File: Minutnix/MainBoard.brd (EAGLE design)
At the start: 222.3 x 73.3 mm, 121 parts, among them IC3 TP4056, IC7 FT232RL, Q4 32.768kHz, X1 FH12-12S-0.5S_THINNER, X2 JST-XH-03-PIN-LONG-PAD, X4 JST-XH-03-PIN-LONG-PAD

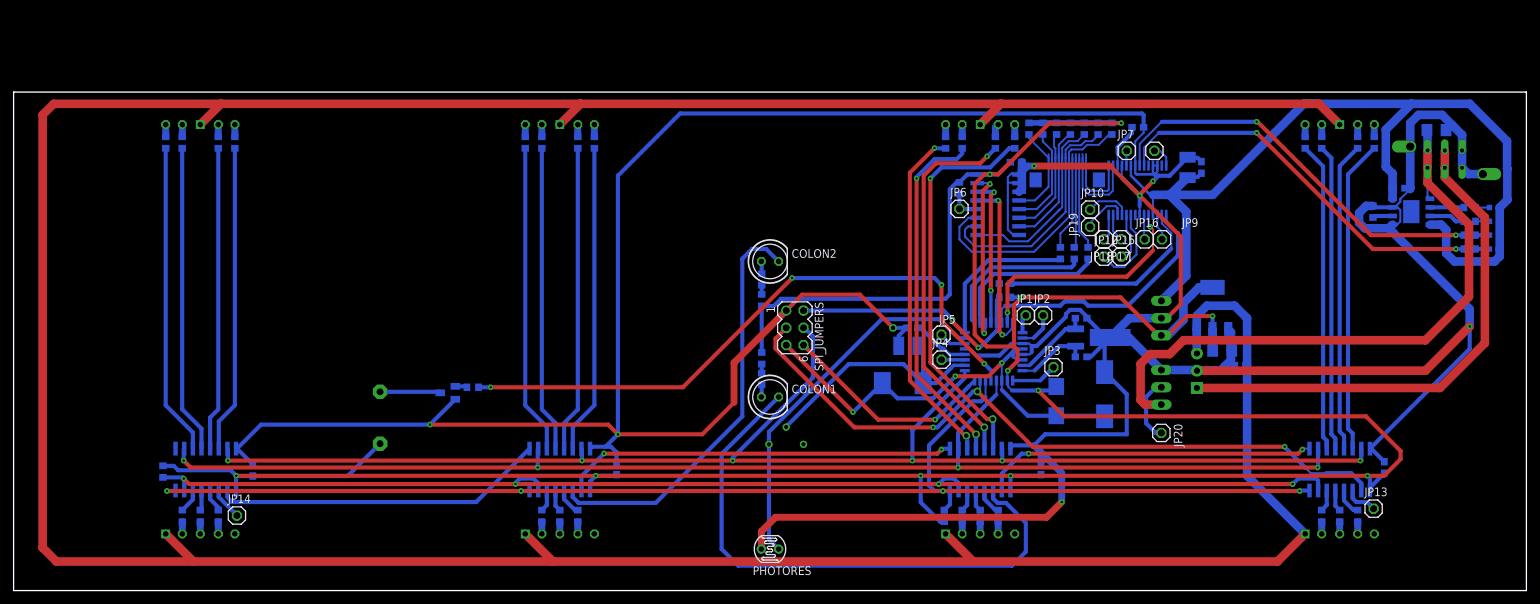
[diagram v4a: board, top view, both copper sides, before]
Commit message: Almost complete
Added 3d extraction
wider better paths
corrected Temperature field of TP to be GND
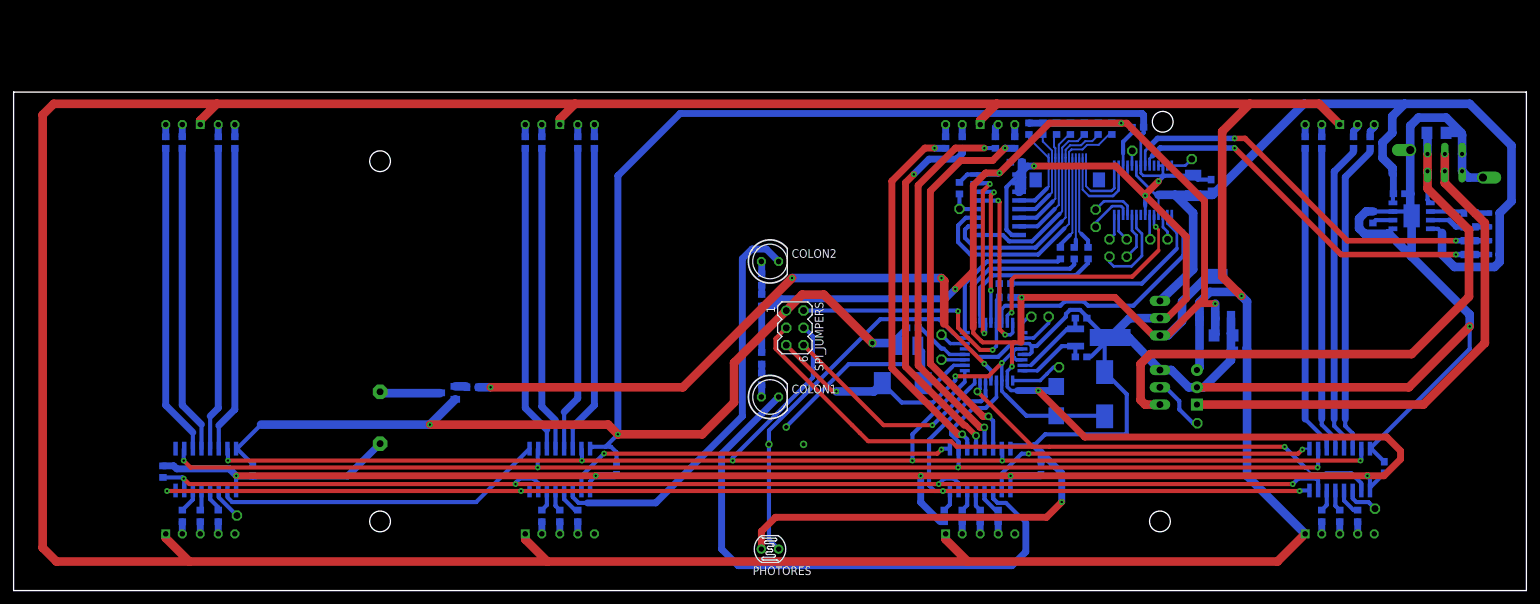
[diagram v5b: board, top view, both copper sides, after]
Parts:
- moved JP8 5.62 mm to (173.1, 63.4), flipped to the bottom
- moved JP20 5.47 mm to (173.9, 24.6), flipped to the bottom
- moved C5 3.00 mm to (176.0, 59.5)
- moved C3 2.76 mm to (173.3, 59.5)
- moved J_REG_9V_1 2.44 mm to (175.2, 29.9)
- moved C7 2.24 mm to (177.8, 37.5)
- moved C6 2.24 mm to (180.2, 35.4)
- moved IC2 1.68 mm to (176.6, 43.1)
- moved JP1 0.84 mm to (149.6, 40.2), flipped to the bottom
- moved JP2 0.84 mm to (152.1, 40.2), flipped to the bottom
- moved IC7 0.81 mm to (166.0, 58.8)
- moved JP12 0.81 mm to (161.0, 49.1), flipped to the bottom
- moved JP18 0.81 mm to (161.0, 51.6), flipped to the bottom
- moved JP3 0.81 mm to (153.6, 32.8), flipped to the bottom
- moved JP7 0.81 mm to (164.4, 64.6), flipped to the bottom
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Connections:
- net GND: now also IC3.ETP
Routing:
- net VDD: track 524.1 -> 559.9 mm, vias 0 -> 1
- net VCC: track 507.3 -> 528.5 mm, vias 11 -> 12
- net D_SI: track 105.2 -> 112.3 mm, vias 3 -> 2
- net GND: track 654.3 -> 661.2 mm
- net +5V: track 147.2 -> 143.6 mm
- net N$36: track 57.6 -> 54.3 mm
- net MS_G: track 51.0 -> 54.2 mm
- net N$43: track 59.1 -> 56.0 mm
- net RESET: track 38.9 -> 41.8 mm
- net MS_F: track 52.4 -> 54.4 mm
- net D_RCK: track 189.6 -> 191.5 mm
- net N$27: track 6.50 -> 8.33 mm
- net ENC_B: track 40.9 -> 42.6 mm
- net S_VCC: track 67.6 -> 66.0 mm
- net BATTERY_S: track 9.51 -> 8.39 mm
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
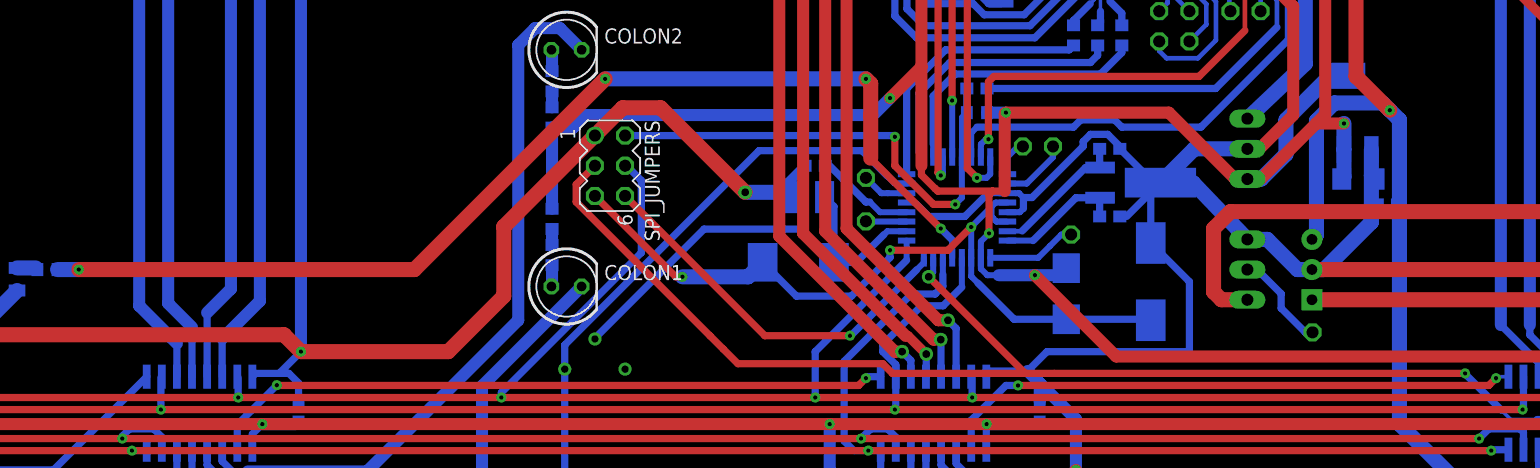
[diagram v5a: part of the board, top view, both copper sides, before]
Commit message: Corrected programmer pins
+ added full inventor 3d model with most important dimensions
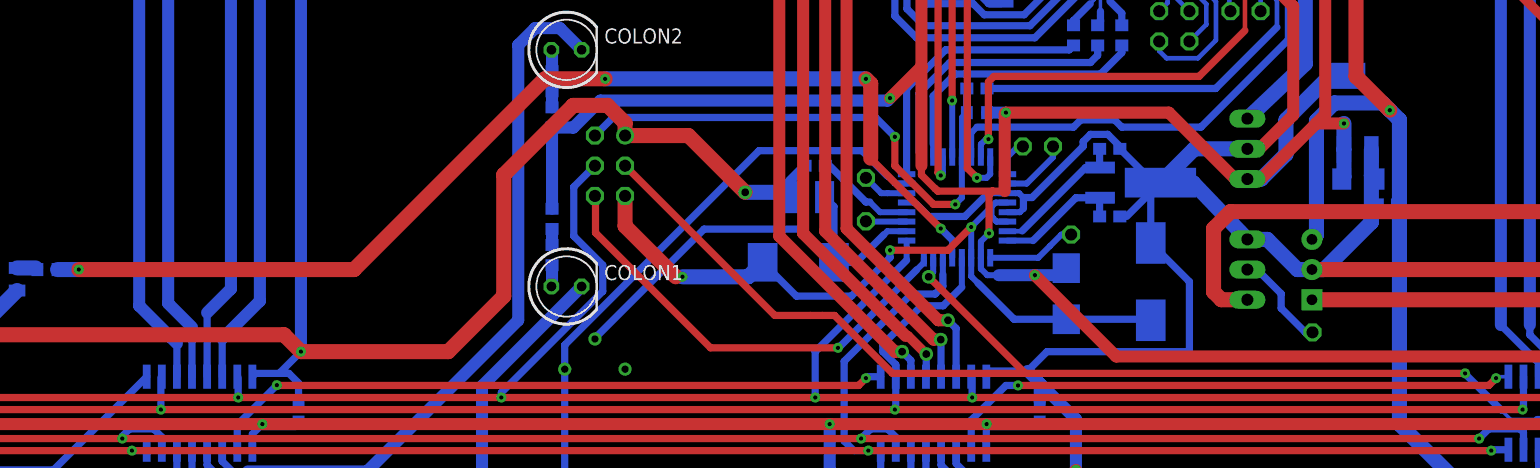
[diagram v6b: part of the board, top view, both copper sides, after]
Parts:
- flipped SPI_JUMPERS to the bottom
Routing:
- net D_SI: track 112.3 -> 105.8 mm
- net MISO: track 33.0 -> 38.1 mm
- net RESET: track 41.8 -> 45.6 mm
- net GND: track 661.2 -> 664.6 mm
- net S_VCC: track 66.0 -> 64.9 mm

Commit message: Revert "Revert "Pools of gnd""
This reverts commit 2f73202806bed85f49afe26d98c16d19bdefccd4.
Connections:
- net GND: now also X1.CASE1, X1.CASE2
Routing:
- net GND: track 664.6 -> 602.3 mm
- net VDD: track 559.9 -> 561.1 mm
- net MS_B: track 57.2 -> 57.8 mm
- net +5V: track 143.6 -> 144.1 mm
- net MS_A: track 56.7 -> 57.2 mm
- net N$43: track 56.0 -> 56.5 mm
- added copper zone on layer 1, net GND
- added copper zone on layer 16, net GND

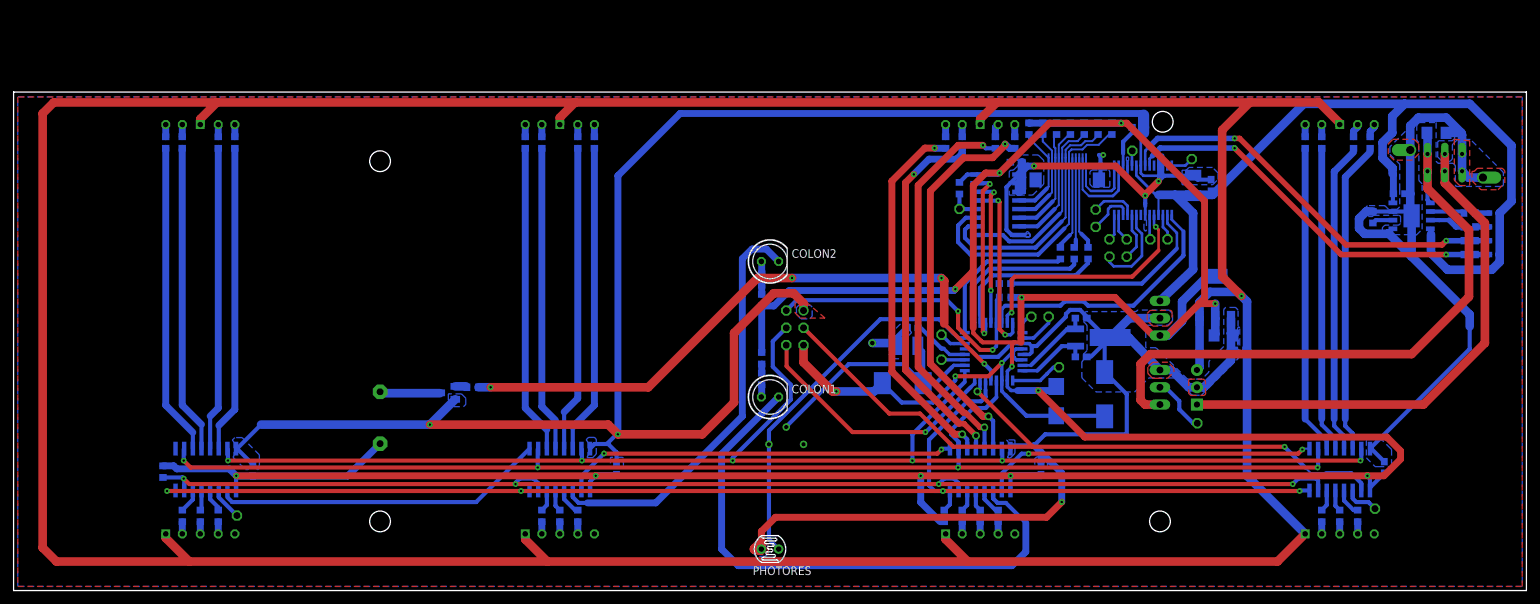
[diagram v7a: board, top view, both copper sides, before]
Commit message: Revert "Pools of gnd"
This reverts commit 4498ba5dce1e14fe788b06c680ced1a0feefa50f.
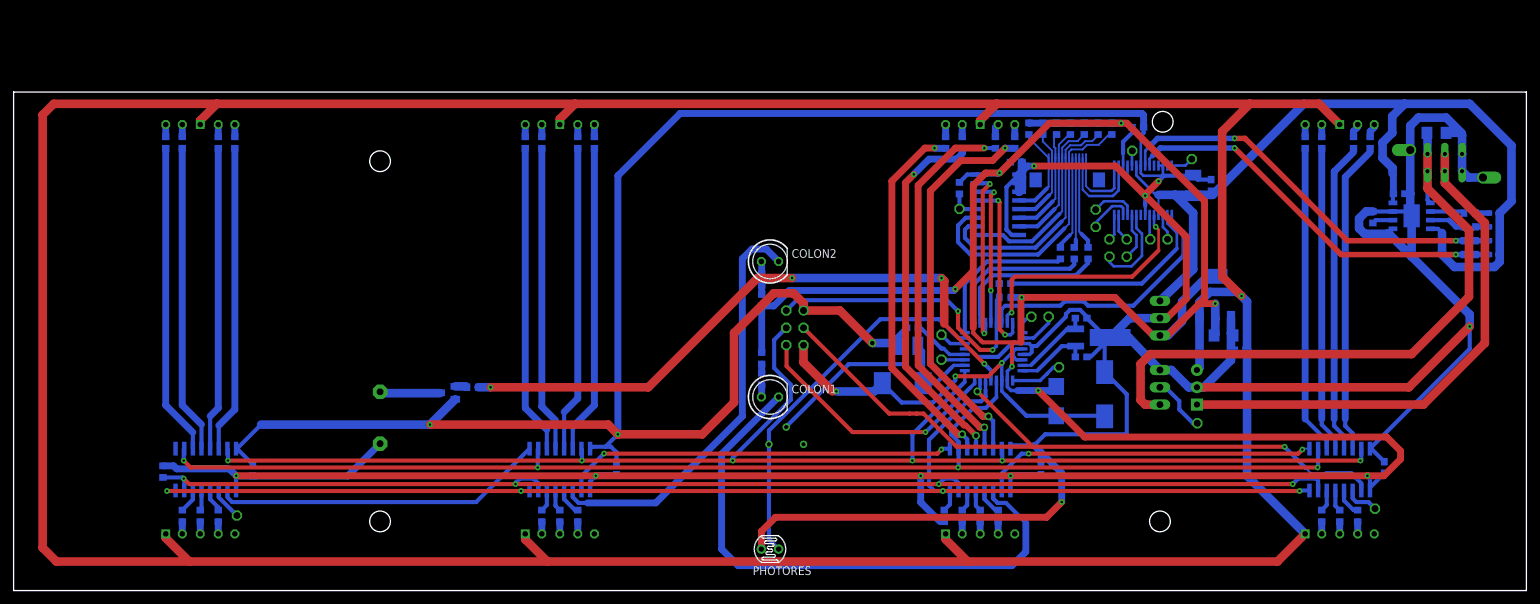
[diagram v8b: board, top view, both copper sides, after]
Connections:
- net GND: no longer X1.CASE1, X1.CASE2
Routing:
- net GND: track 602.3 -> 664.6 mm
- net VDD: track 561.1 -> 559.9 mm
- net MS_B: track 57.8 -> 57.2 mm
- net +5V: track 144.1 -> 143.6 mm
- net MS_A: track 57.2 -> 56.7 mm
- net N$43: track 56.5 -> 56.0 mm
- removed copper zone on layer 1, net GND
- removed copper zone on layer 16, net GND
